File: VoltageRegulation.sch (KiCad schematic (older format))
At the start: 55 parts, among them Q201 TIP41, Q202 TIP41, Q203 TIP42, U201 LM7812_TO220, U202 LM7805_TO220, U203 Step Down Module +15 to 7v - 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, U204 LM7912_TO220, U205 XL6009 Module DCDC 19 to 30v, U206 TL071, U207 LM78M05_TO252, U208 LM78M12_TO252, U209 MC79M12_TO252, U210 MT3608 Module DCDC 19 to 28v

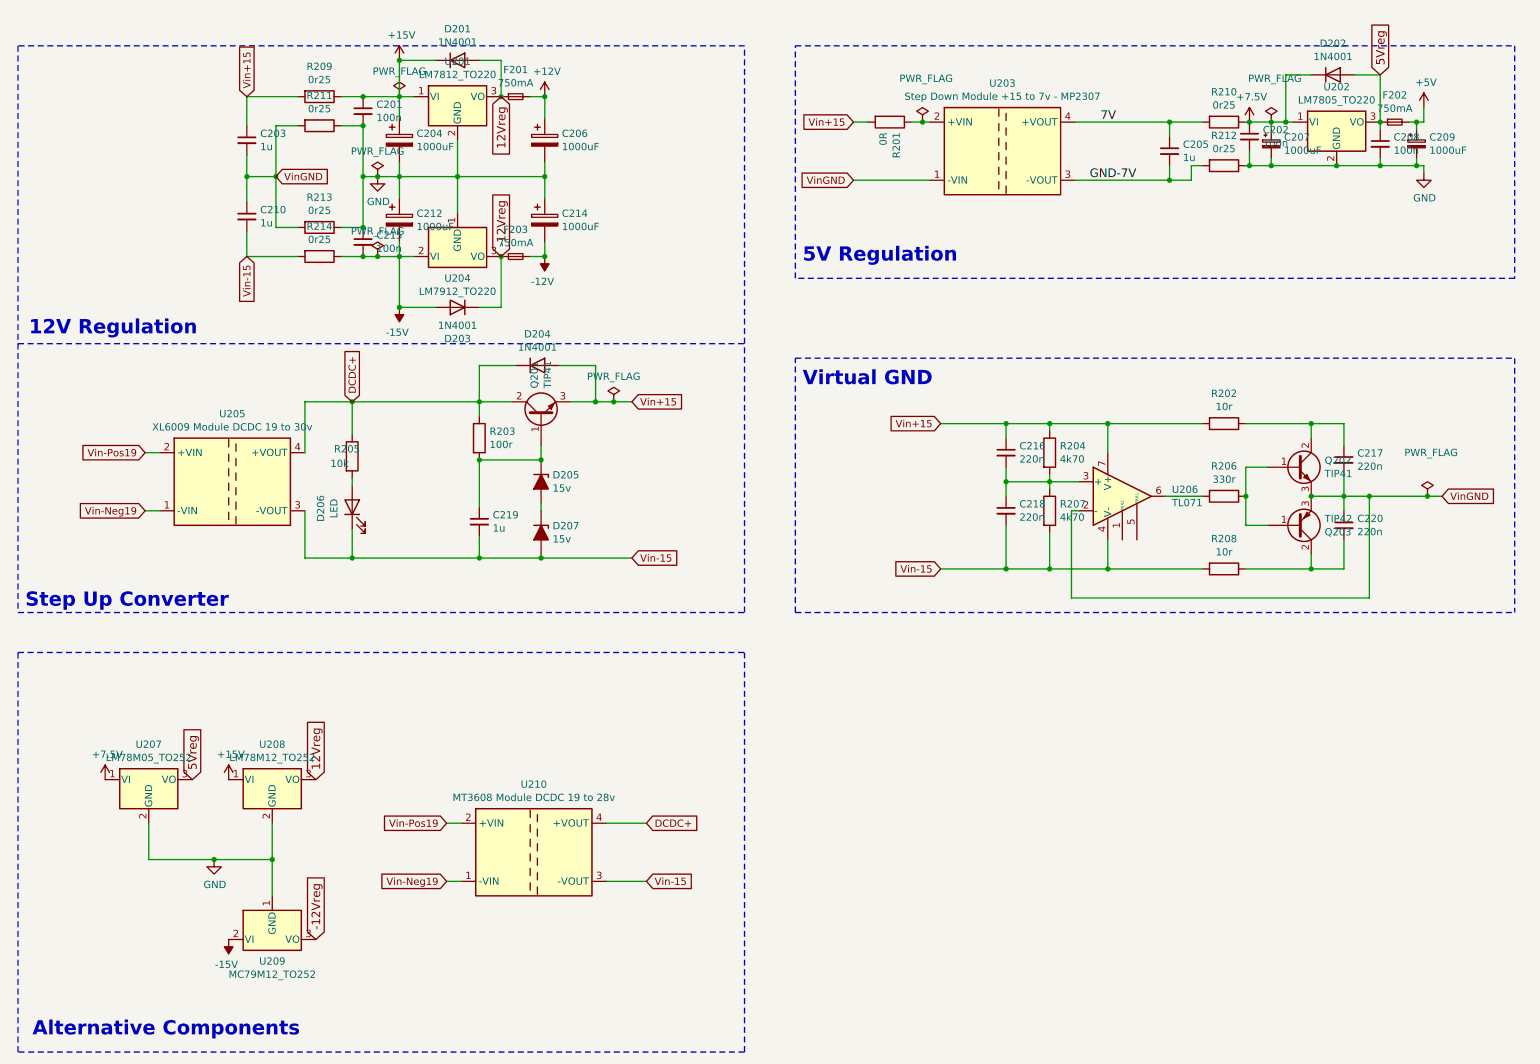
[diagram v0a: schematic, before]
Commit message: Init 750mA indicator
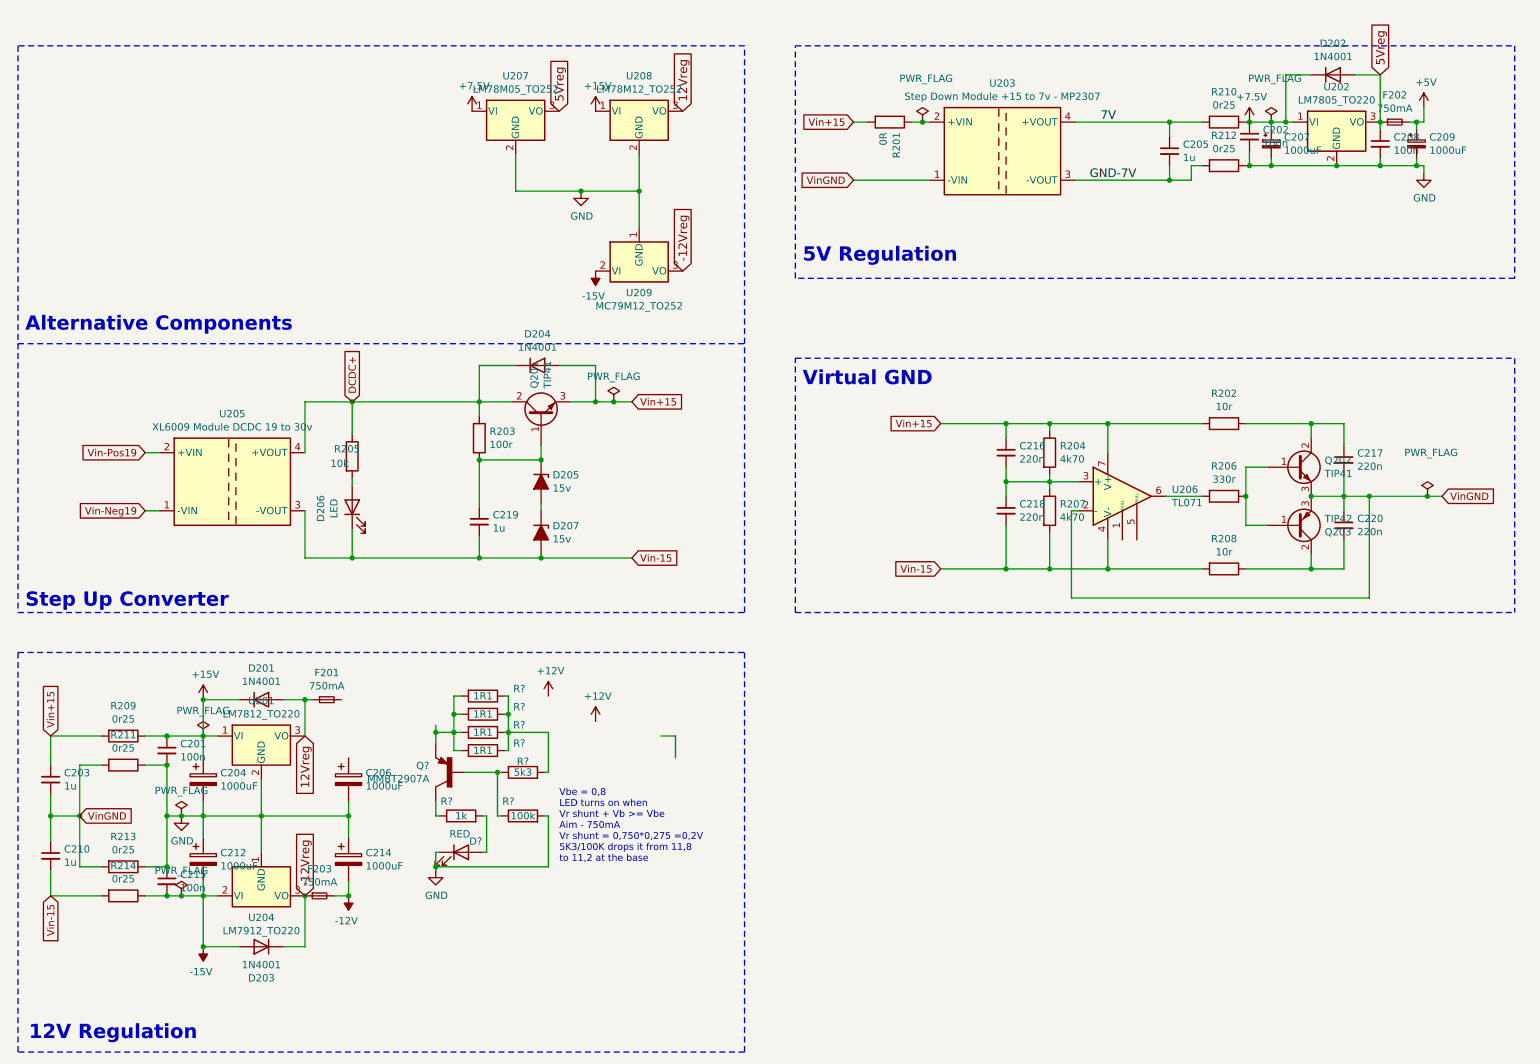
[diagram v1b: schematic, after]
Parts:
- removed U210: MT3608 Module DCDC 19 to 28v, AJ:MT3608 DCDC-Module-USB, symbol Regulator_Switching:CRE1S1205SC
- added D?: RED, LED_THT:LED_D5.0mm, symbol Device:LED
- added Q?: MMBT2907A, symbol MMBT2907A:MMBT2907A
- added R? (x4): 1R1, Resistor_SMD:R_0805_2012Metric_Pad1.15x1.40mm_HandSolder, symbol Device:R
- added R?: 1k, Resistor_SMD:R_0805_2012Metric_Pad1.15x1.40mm_HandSolder, symbol Device:R
- added R?: 5k3, Resistor_SMD:R_0805_2012Metric_Pad1.15x1.40mm_HandSolder, symbol Device:R
- added R?: 100k, Resistor_SMD:R_0805_2012Metric_Pad1.15x1.40mm_HandSolder, symbol Device:R
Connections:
- net +12V: no longer C206.1, F201.2
- net GND: now also D?.1 (K), R?.2
- new net: Q?.B, R?.1, R?.1
- new net: Q?.C, R?.1
- new net: Q?.E, R?.2, R?.2, R?.2, R?.2
- new net: R?.1, R?.1, R?.1, R?.1, R?.2
- new net: D?.2 (A), R?.2
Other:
- note added: "Vbe = 0,8\nLED turns on when \nVr shunt + Vb >= Vbe\nAim - 750mA\nVr shunt = 0,750*0,275 =0,2V \n5K3/100K drops it from 11,8 \nto 11,2 at the base"
- moved on the sheet: C201, C203, C204, C206, C210, C212, C214, C215, D201, D203, F201, F203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

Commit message: 5V current sensor
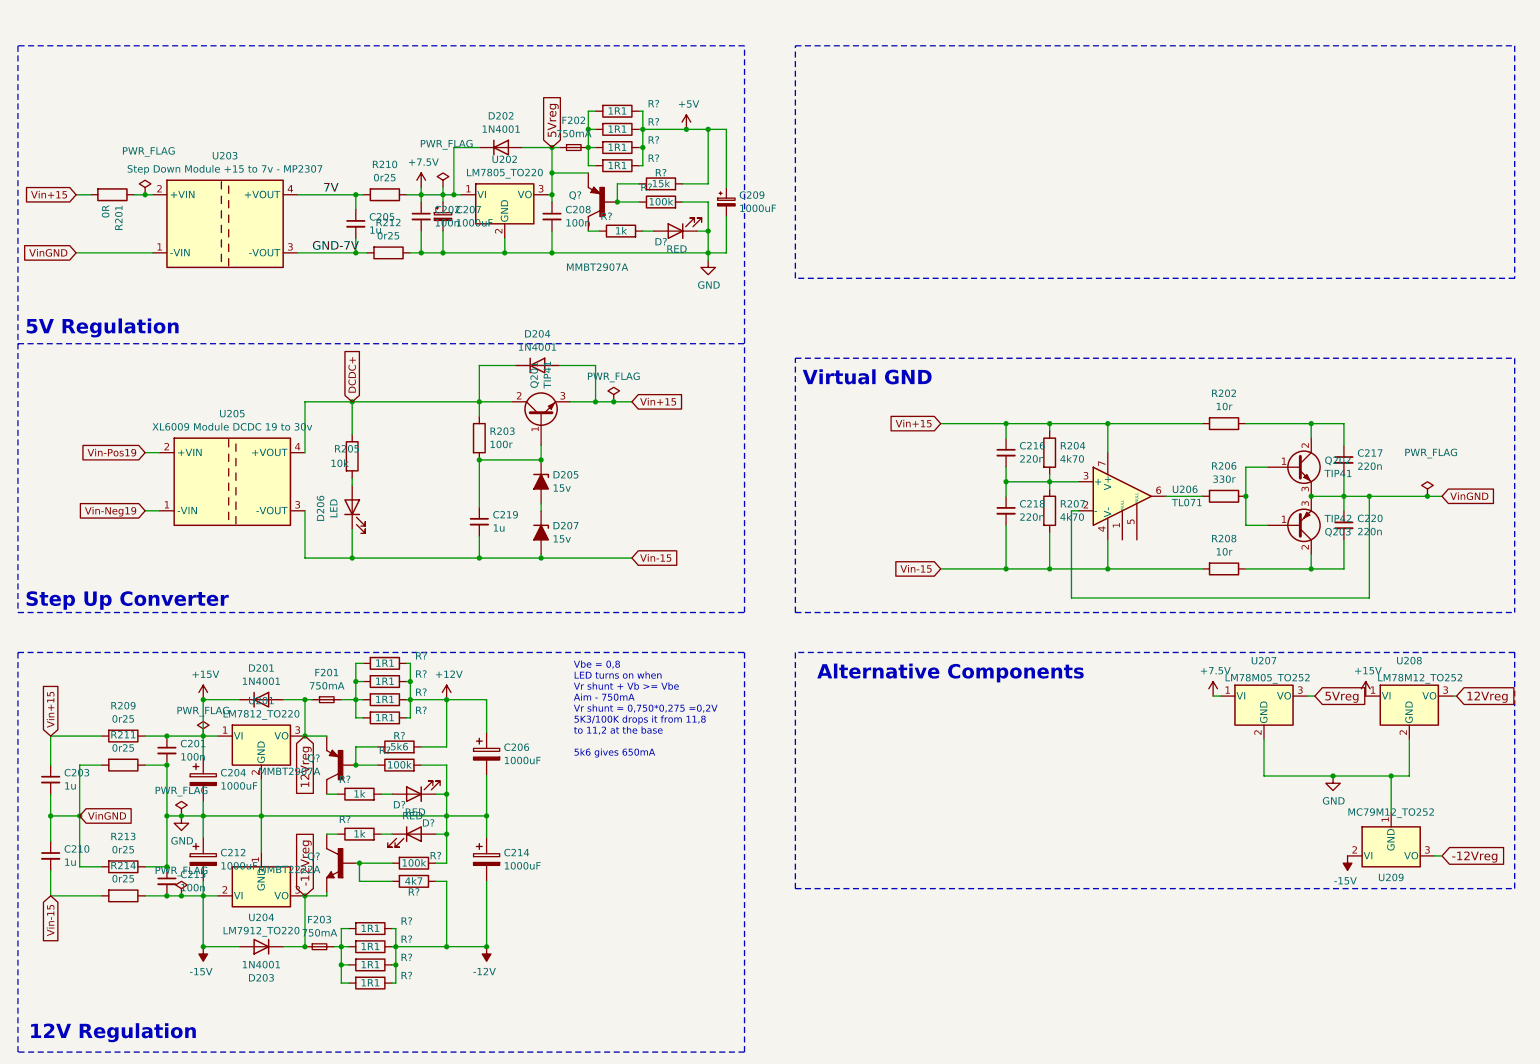
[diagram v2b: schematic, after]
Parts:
- added D? (x2): RED, LED_THT:LED_D5.0mm, symbol Device:LED
- added Q?: MMBT2222A, SOT23, symbol MMBT2222A:MMBT2222A
- added Q?: MMBT2907A, symbol MMBT2907A:MMBT2907A
- added R? (x8): 1R1, Resistor_SMD:R_0805_2012Metric_Pad1.15x1.40mm_HandSolder, symbol Device:R
- added R? (x2): 1k, Resistor_SMD:R_0805_2012Metric_Pad1.15x1.40mm_HandSolder, symbol Device:R
- added R?: 4k7, Resistor_SMD:R_0805_2012Metric_Pad1.15x1.40mm_HandSolder, symbol Device:R
- added R? (x2): 100k, Resistor_SMD:R_0805_2012Metric_Pad1.15x1.40mm_HandSolder, symbol Device:R
- added R?: 15k, Resistor_SMD:R_0805_2012Metric_Pad1.15x1.40mm_HandSolder, symbol Device:R
- R?: value 5k3 -> 5k6
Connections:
- net +12V: now also C206.1, R?.1, R?.1, R?.1, R?.1, R?.2
- net +5V: now also R?.1, R?.1, R?.1, R?.1, R?.2; no longer F202.2
- net -12V: now also R?.1, R?.1, R?.1, R?.1, R?.1; no longer F203.2
- net -12Vreg: now also Q?.2 (E)
- net 12Vreg: now also Q?.E
- net 5Vreg: now also Q?.E
- net GND: now also D?.1 (K), D?.2 (A), R?.1, R?.2
- net at F201.2: now also R?.2, R?.2, R?.2, R?.2
- new net: F203.2, R?.2, R?.2, R?.2, R?.2
- new net: F202.2, R?.2, R?.2, R?.2, R?.2
- new net: Q?.3 (C), R?.1
- new net: D?.1 (K), R?.2
- new net: Q?.1 (B), R?.2, R?.2
- new net: Q?.B, R?.1, R?.1
- new net: Q?.C, R?.1
- new net: D?.2 (A), R?.2
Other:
- note added: "Vbe = 0,8\nLED turns on when \nVr shunt + Vb >= Vbe\nAim - 750mA\nVr shunt = 0,750*0,275 =0,2V \n5K3/100K drops it from 11,8 \nto 11,2 at the base \n\n5k6 gives 650mA"
- note removed: "Vbe = 0,8\nLED turns on when \nVr shunt + Vb >= Vbe\nAim - 750mA\nVr shunt = 0,750*0,275 =0,2V \n5K3/100K drops it from 11,8 \nto 11,2 at the base"
- moved on the sheet: C202, C205, C206, C207, C208, C209, C214, D202, D?, F202, F203, Q?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

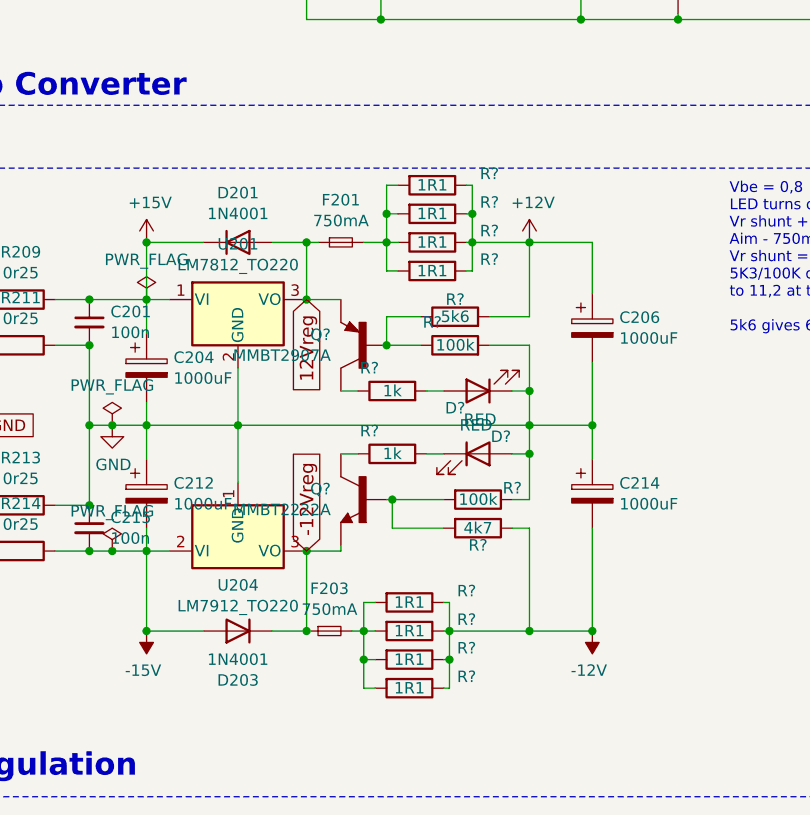
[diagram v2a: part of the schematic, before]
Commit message: Jumper before/after fuse
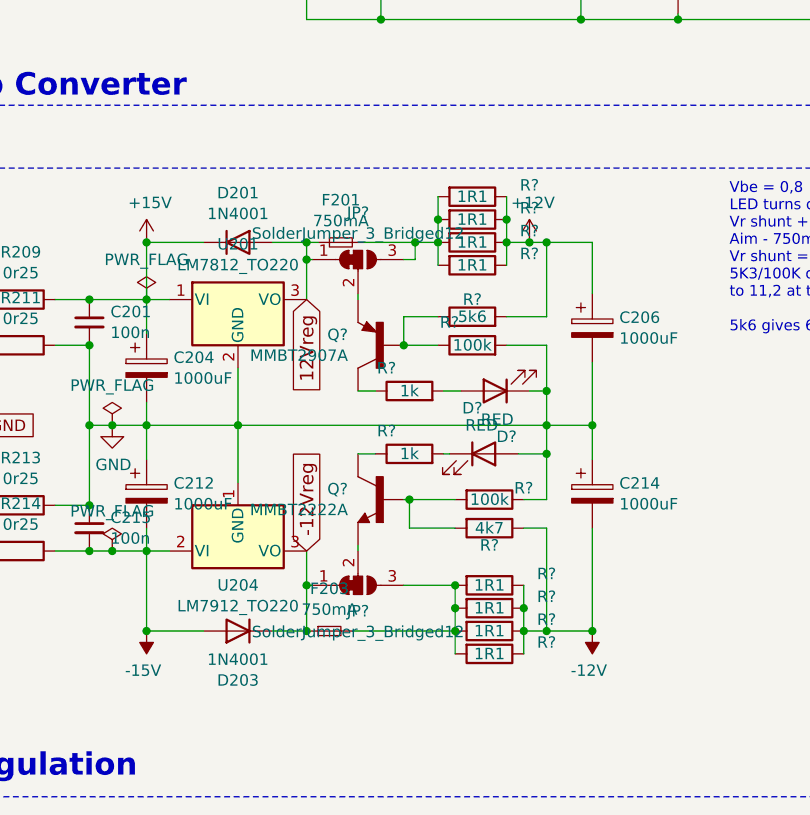
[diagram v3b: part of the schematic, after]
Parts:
- removed R? (x4): 1R1, Resistor_SMD:R_0805_2012Metric_Pad1.15x1.40mm_HandSolder, symbol Device:R
- added JP? (x2): SolderJumper_3_Bridged12, symbol Jumper:SolderJumper_3_Bridged12
- added R? (x4): 1R1, Resistor_SMD:R_0805_2012Metric_Pad1.15x1.40mm_HandSolder, symbol Device:R
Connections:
- net -12V: now also R?.1, R?.1, R?.1, R?.1
- net -12Vreg: now also JP?.1 (A); no longer Q?.2 (E)
- net 12Vreg: now also JP?.1 (A); no longer Q?.E
- net at F203.2: now also JP?.3 (B), R?.2, R?.2, R?.2, R?.2
- net at F201.2, R?.2, R?.2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: now also JP?.3 (B)
- new net: JP?.2 (C), Q?.E
- new net: JP?.2 (C), Q?.2 (E)
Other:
- moved on the sheet: D?, Q?, R?
